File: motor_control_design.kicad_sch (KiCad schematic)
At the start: 90 parts, among them J1 TYPE-C-31-M-12, J10 5V, J2 SWD, J3 VBAT, J4 GND, J5 FC_M/P, J6 Conn_01x06, J7 Conn_01x04_Pin, J8 Conn_01x06, J9 GND, Q1 RF1S9540SM, Q10 2N7002, Q11 2N7002, Q12 2N7002, Q13 2N7002, Q14 RF1S9540SM, Q15 IRLZ44NS, Q16 2N7002, Q2 RF1S9540SM, Q3 IRLZ44NS, Q4 2N7002, Q5 2N7002, Q6 RF1S9540SM, Q7 IRLZ44NS, Q8 2N7002, Q9 IRLZ44NS, U1 STM32F401CCU6, U2 LT1962-3.3, U4 TPS563200, Y1 16MHz

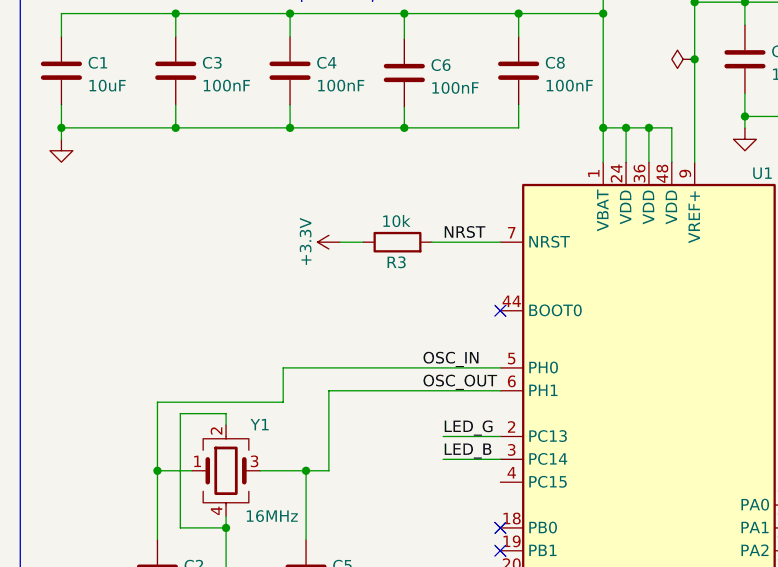
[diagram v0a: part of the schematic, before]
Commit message: cleaned up NRST BOOT0 schematic
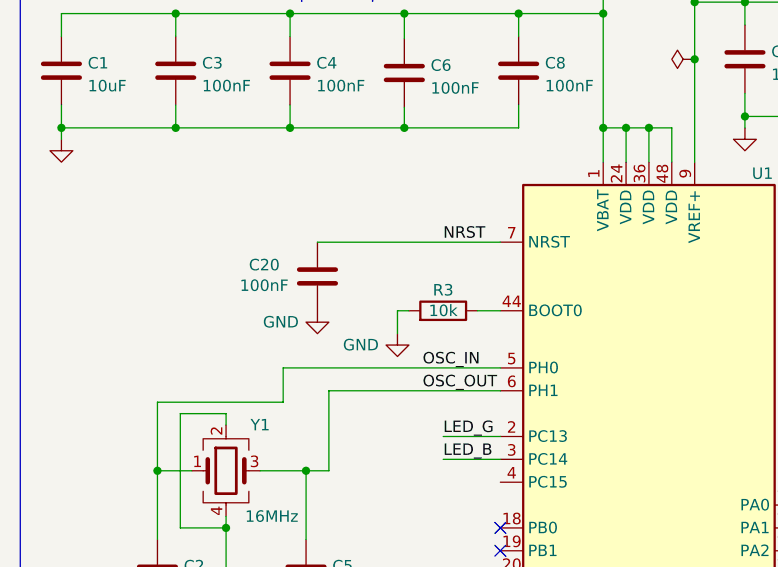
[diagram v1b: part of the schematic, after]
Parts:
- added C20: 100nF, symbol Device:C
- R3: LCSC Part C176114 -> C174364
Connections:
- net +3.3V: no longer R3.1
- net GND: now also R3.2, C20.2
- net NRST: now also C20.1; no longer R3.2
- net at U1.44 (BOOT0): now also R3.1
- no-connect marks 14 -> 13

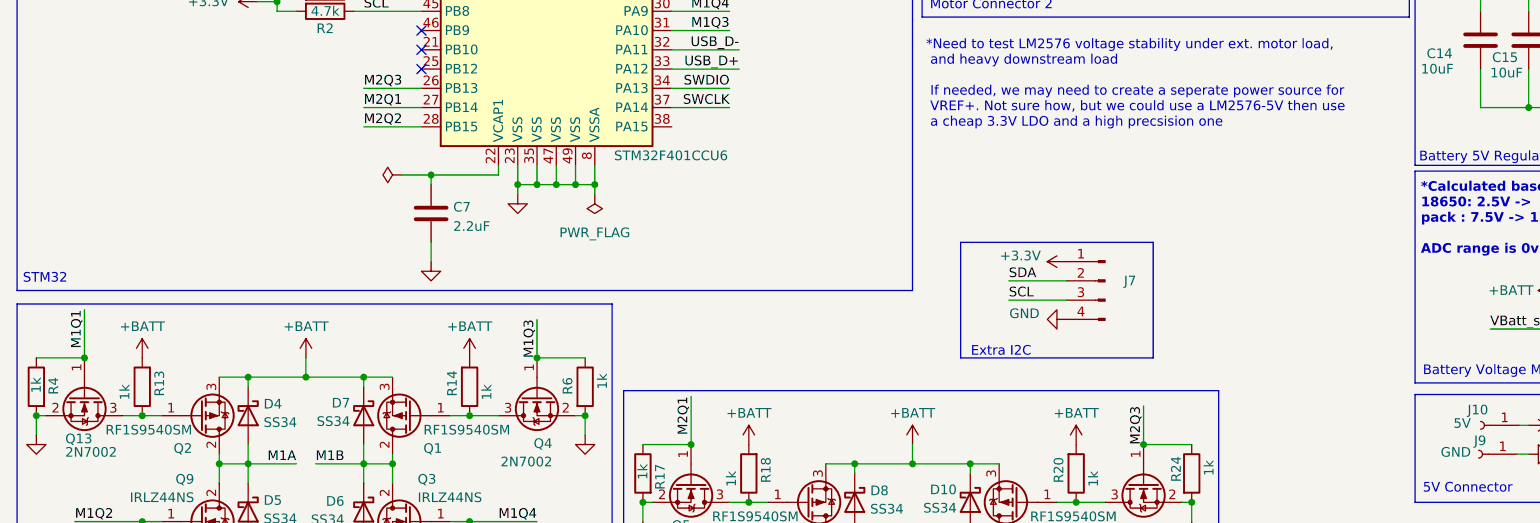
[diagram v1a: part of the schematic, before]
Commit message: Added LTC4365
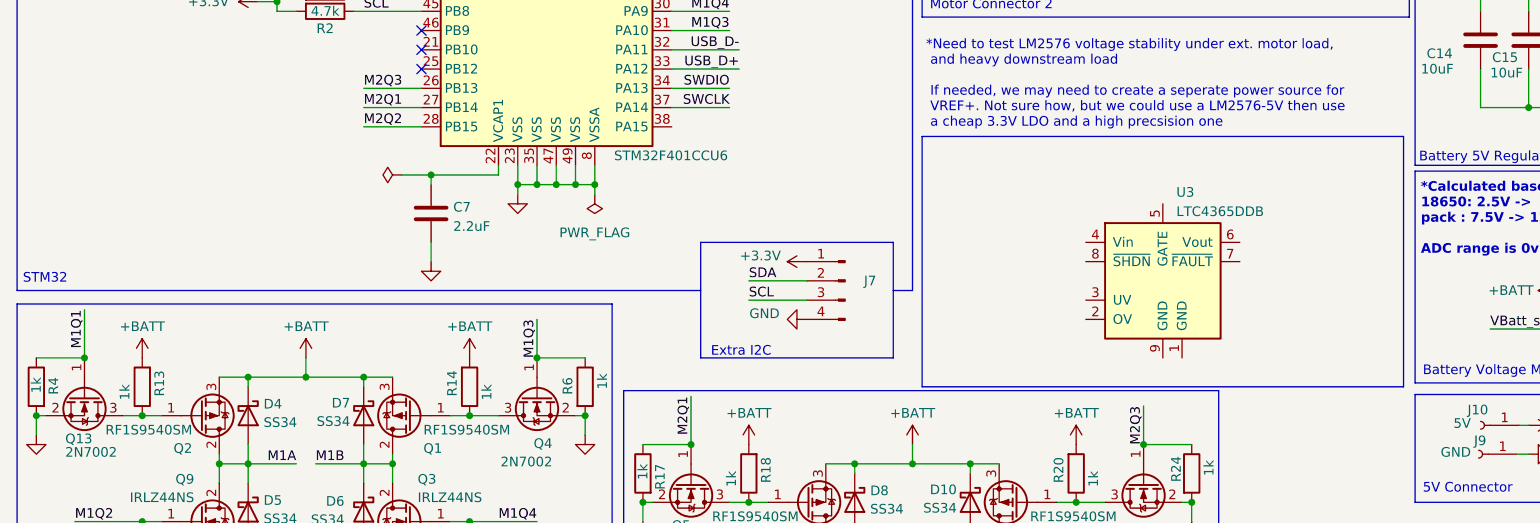
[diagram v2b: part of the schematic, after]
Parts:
- added U3: LTC4365DDB, Package_DFN_QFN:DFN-8-1EP_2x3mm_P0.5mm_EP0.61x2.2mm, symbol Power_Management:LTC4365DDB
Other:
- moved on the sheet: J7
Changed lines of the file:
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@@
 	)
 	(rectangle
+		(start 133.35 116.84)
+		(end 196.85 149.86)
+		(stroke
+			(width 0)
+			(type default)
+		)
+		(fill
+			(type none)
+		)
+	)
+	(rectangle
 		(start 133.35 68.58)
 		(end 197.612 101.092)
@@
 		)
 	)
-	(rectangle
-		(start 13.97 13.97)
-		(end 132.08 137.16)
-		(stroke
-			(width 0)
-			(type default)
-		)
-		(fill
-			(type none)
-		)
-	)
 	(text "Battery 5V Regulator"
 		(exclude_from_sim no)
@@
 	(text "Extra I2C\n"
 		(exclude_from_sim no)
-		(at 143.764 145.288 0)
+		(at 109.474 145.288 0)
 		(effects
 			(font
@@
 		)
 	)
+	(polyline
+		(pts
+			(xy 13.97 13.97) (xy 132.08 13.97)
+		)
+		(stroke
+			(width 0)
+			(type default)
+		)
+	)
 	(wire
 		(pts
@@
 	(wire
 		(pts
-			(xy 144.78 138.43) (xy 152.4 138.43)
+			(xy 110.49 138.43) (xy 118.11 138.43)
 		)
 		(stroke
@@
 	(polyline
 		(pts
-			(xy 138.43 146.05) (xy 163.83 146.05)
+			(xy 104.14 146.05) (xy 129.54 146.05)
 		)
 		(stroke
@@
 	(polyline
 		(pts
-			(xy 138.43 130.81) (xy 163.83 130.81)
+			(xy 104.14 130.81) (xy 129.54 130.81)
 		)
 		(stroke
@@
 		)
 	)
+	(polyline
+		(pts
+			(xy 13.97 137.16) (xy 104.14 137.16)
+		)
+		(stroke
+			(width 0)
+			(type default)
+		)
+	)
 	(wire
 		(pts
@@
 		)
 	)
+	(polyline
+		(pts
+			(xy 129.54 137.16) (xy 132.08 137.16)
+		)
+		(stroke
+			(width 0)
+			(type default)
+		)
+	)
 	(wire
 		(pts
@@
 	(wire
 		(pts
-			(xy 144.78 135.89) (xy 152.4 135.89)
+			(xy 110.49 135.89) (xy 118.11 135.89)
 		)
 		(stroke
@@
 		)
 	)
+	(polyline
+		(pts
+			(xy 13.97 137.16) (xy 13.97 13.97)
+		)
+		(stroke
+			(width 0)
+			(type default)
+		)
+	)
 	(wire
 		(pts
@@
 		)
 	)
+	(polyline
+		(pts
+			(xy 132.08 13.97) (xy 132.08 137.16)
+		)
+		(stroke
+			(width 0)
+			(type default)
+		)
+	)
 	(wire
 		(pts
@@
 	(polyline
 		(pts
-			(xy 138.43 130.81) (xy 138.43 146.05)
+			(xy 104.14 130.81) (xy 104.14 146.05)
 		)
 		(stroke
@@
 	(polyline
 		(pts
-			(xy 163.83 146.05) (xy 163.83 130.81)
+			(xy 129.54 146.05) (xy 129.54 130.81)
 		)
 		(stroke
@@
 	)
 	(label "SCL"
-		(at 144.78 138.43 0)
+		(at 110.49 138.43 0)
 		(effects
 			(font
@@
 	)
 	(label "SDA"
-		(at 144.78 135.89 0)
+		(at 110.49 135.89 0)
 		(effects
 			(font
@@
 	)
 	(symbol
+		(lib_id "Power_Management:LTC4365DDB")
+		(at 165.1 135.89 0)
+		(unit 1)
+		(exclude_from_sim no)
+		(in_bom yes)
+		(on_board yes)
+		(dnp no)
+		(property "Reference" "U3"
+			(at 166.878 124.206 0)
+			(effects
+				(font
+					(size 1.27 1.27)
+				)
+				(justify left)
+			)
+		)
+		(property "Value" "LTC4365DDB"
+			(at 166.878 126.746 0)
+			(effects
+				(font
+					(size 1.27 1.27)
+				)
+				(justify left)
+			)
+		)
+		(property "Footprint" "Package_DFN_QFN:DFN-8-1EP_2x3mm_P0.5mm_EP0.61x2.2mm"
+			(at 165.1 148.59 0)
+			(effects
+				(font
+					(size 1.27 1.27)
+				)
+				(hide yes)
+			)
+		)
+		(property "Datasheet" "https://www.analog.com/media/en/technical-documentation/data-sheets/4365fa.pdf"
+			(at 165.1 133.35 0)
+			(effects
+				(font
+					(size 1.27 1.27)
+				)
+				(hide yes)
+			)
+		)
+		(property "Description" "UV, OV and Reverse Supply Protection Controller, 50/60Hz noise rejection, DFN-8"
+			(at 165.1 135.89 0)
+			(effects
+				(font
+					(size 1.27 1.27)
+				)
+				(hide yes)
+			)
+		)
+		(pin "4"
+		)
+		(pin "3"
+		)
+		(pin "8"
+		)
+		(pin "6"
+		)
+		(pin "9"
+		)
+		(pin "7"
+		)
+		(pin "1"
+		)
+		(pin "5"
+		)
+		(pin "2"
+		)
+		(instances
+			(project ""
+				(path "/e96577c4-ec21-4b26-996c-9ebc38d9c737"
+					(reference "U3")
+					(unit 1)
+				)
+			)
+		)
+	)
+	(symbol
 		(lib_id "power:GND")
 		(at 144.78 91.44 90)
@@
 	(symbol
 		(lib_id "Connector:Conn_01x04_Pin")
-		(at 157.48 135.89 0)
+		(at 123.19 135.89 0)
 		(mirror y)
 		(unit 1)
@@
 		(dnp no)
 		(property "Reference" "J7"
-			(at 160.782 135.89 0)
+			(at 126.492 135.89 0)
 			(effects
 				(font
@@
 		)
 		(property "Value" "Conn_01x04_Pin"
-			(at 156.845 130.81 0)
+			(at 122.555 130.81 0)
 			(effects
 				(font
@@
 		)
 		(property "Footprint" "Connector_JST:JST_SH_BM04B-SRSS-TB_1x04-1MP_P1.00mm_Vertical"
-			(at 157.48 135.89 0)
+			(at 123.19 135.89 0)
 			(effects
 				(font
@@
 		)
 		(property "Datasheet" "~"
-			(at 157.48 135.89 0)
+			(at 123.19 135.89 0)
 			(effects
 				(font
@@
 		)
 		(property "Description" "Generic connector, single row, 01x04, script generated"
-			(at 157.48 135.89 0)
+			(at 123.19 135.89 0)
 			(effects
 				(font
@@
 		)
 		(property "LCSC Part" "C160390"
-			(at 157.48 135.89 0)
+			(at 123.19 135.89 0)
 			(effects
 				(font
@@
 	(symbol
 		(lib_id "power:+3.3V")
-		(at 152.4 133.35 90)
+		(at 118.11 133.35 90)
 		(mirror x)
 		(unit 1)
@@
 		(dnp no)
 		(property "Reference" "#PWR031"
-			(at 156.21 133.35 0)
+			(at 121.92 133.35 0)
 			(effects
 				(font
@@
 		)
 		(property "Value" "+3.3V"
-			(at 146.304 132.588 90)
+			(at 112.014 132.588 90)
 			(effects
 				(font
@@
 		)
 		(property "Footprint" ""
-			(at 152.4 133.35 0)
+			(at 118.11 133.35 0)
 			(effects
 				(font
@@
 		)
 		(property "Datasheet" ""
-			(at 152.4 133.35 0)
+			(at 118.11 133.35 0)
 			(effects
 				(font
@@
 		)
 		(property "Description" ""
-			(at 152.4 133.35 0)
+			(at 118.11 133.35 0)
 			(effects
 				(font
@@
 		(lib_name "GND_6")
 		(lib_id "power:GND")
-		(at 152.4 140.97 270)
+		(at 118.11 140.97 270)
 		(unit 1)
 		(exclude_from_sim no)
@@
 		(dnp no)
 		(property "Reference" "#PWR032"
-			(at 146.05 140.97 0)
+			(at 111.76 140.97 0)
 			(effects
 				(font
@@
 		)
 		(property "Value" "GND"
-			(at 148.844 140.208 90)
+			(at 114.554 140.208 90)
 			(effects
 				(font
@@
 		)
 		(property "Footprint" ""
-			(at 152.4 140.97 0)
+			(at 118.11 140.97 0)
 			(effects
 				(font
@@
 		)
 		(property "Datasheet" ""
-			(at 152.4 140.97 0)
+			(at 118.11 140.97 0)
 			(effects
 				(font
@@
 		)
 		(property "Description" "Power symbol creates a global label with name \"GND\" , ground"
-			(at 152.4 140.97 0)
+			(at 118.11 140.97 0)
 			(effects
 				(font

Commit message: Overvoltage system schematic drafted
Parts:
- added R29, R30: R, symbol Device:R
- added U5: SSM6N7002KFU_LF, SOT-363 US6_TOS, symbol Custom:SSM6N7002KFU_LF
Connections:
- net +BATT: now also U3.3 (UV), U3.4 (Vin), R29.1, U5.3 (DRAIN2); no longer D4.1 (K), D7.1 (K), Q1.3 (S), Q2.3 (S), R18.2
- net GND: now also U3.1 (GND), U3.9 (GND), R30.2
- net at U3.2 (OV): now also R29.2, R30.1
- net at U3.5 (GATE): now also U5.2 (GATE1), U5.5 (GATE2)
- net at U3.6 (Vout): now also U5.6 (DRAIN1)
- new net: D4.1 (K), D7.1 (K), Q1.3 (S), Q2.3 (S)
- new net: U5.1 (SOURCE1), U5.4 (SOURCE2)
- no-connect marks 13 -> 14
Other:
- note removed: "*Need to test LM2576 voltage stability under ext. motor load, and heavy downstream load If needed, we may need to create a seperate power source for VREF+. Not sure how, but we could use a LM2576-5V then use a cheap 3.3V LDO and a high precsision one"
- moved on the sheet: U3

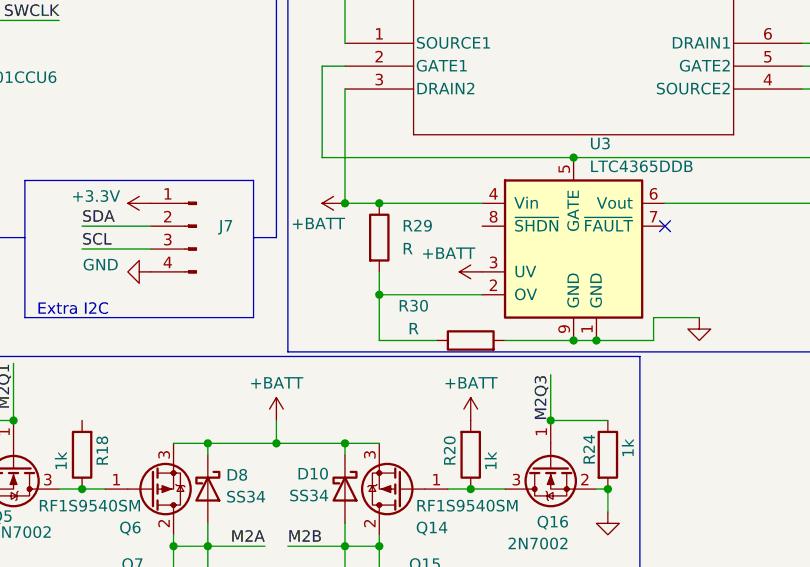
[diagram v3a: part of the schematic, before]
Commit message: updated overvoltage resistor values
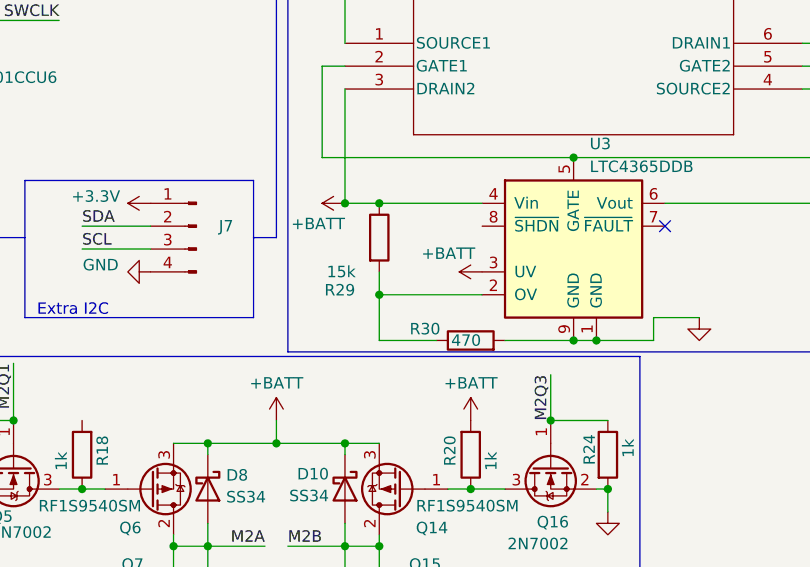
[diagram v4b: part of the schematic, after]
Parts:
- R29: value R -> 15k
- R30: value R -> 470
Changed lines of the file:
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@@
 		(on_board yes)
 		(dnp no)
-		(fields_autoplaced yes)
 		(property "Reference" "R29"
-			(at 146.05 135.8899 0)
-			(effects
-				(font
-					(size 1.27 1.27)
-				)
-				(justify left)
-			)
-		)
-		(property "Value" "R"
-			(at 146.05 138.4299 0)
+			(at 137.414 143.002 0)
+			(effects
+				(font
+					(size 1.27 1.27)
+				)
+				(justify left)
+			)
+		)
+		(property "Value" "15k"
+			(at 137.668 140.97 0)
 			(effects
 				(font
@@
 		(dnp no)
 		(property "Reference" "R30"
-			(at 147.32 144.78 90)
-			(effects
-				(font
-					(size 1.27 1.27)
-				)
-			)
-		)
-		(property "Value" "R"
-			(at 147.32 147.32 90)
-			(effects
-				(font
+			(at 148.59 147.32 90)
+			(effects
+				(font
+					(size 1.27 1.27)
+				)
+			)
+		)
+		(property "Value" "470"
+			(at 153.162 148.59 90)
+			(effects
+				(font

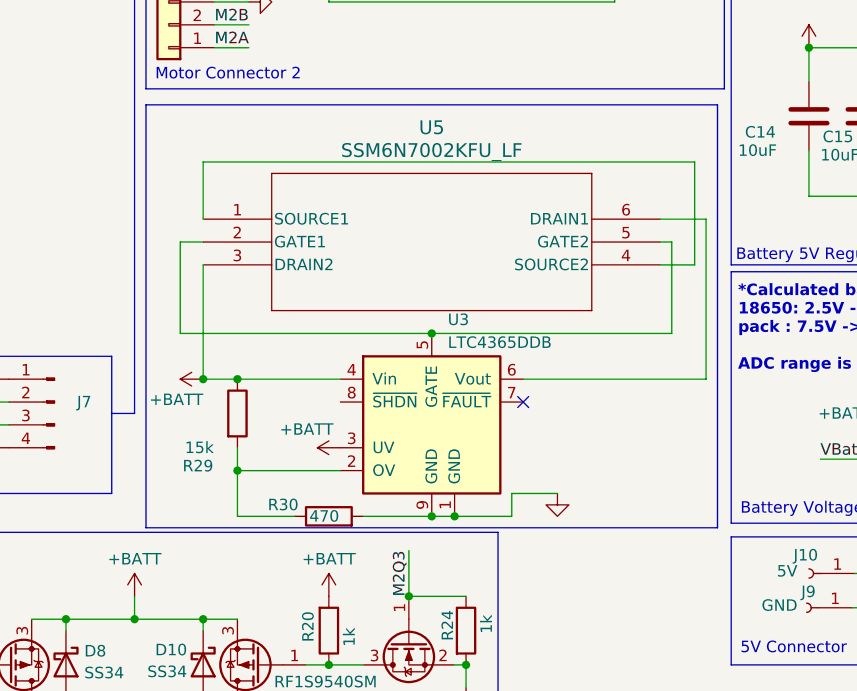
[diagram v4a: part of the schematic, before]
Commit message: connected shdn
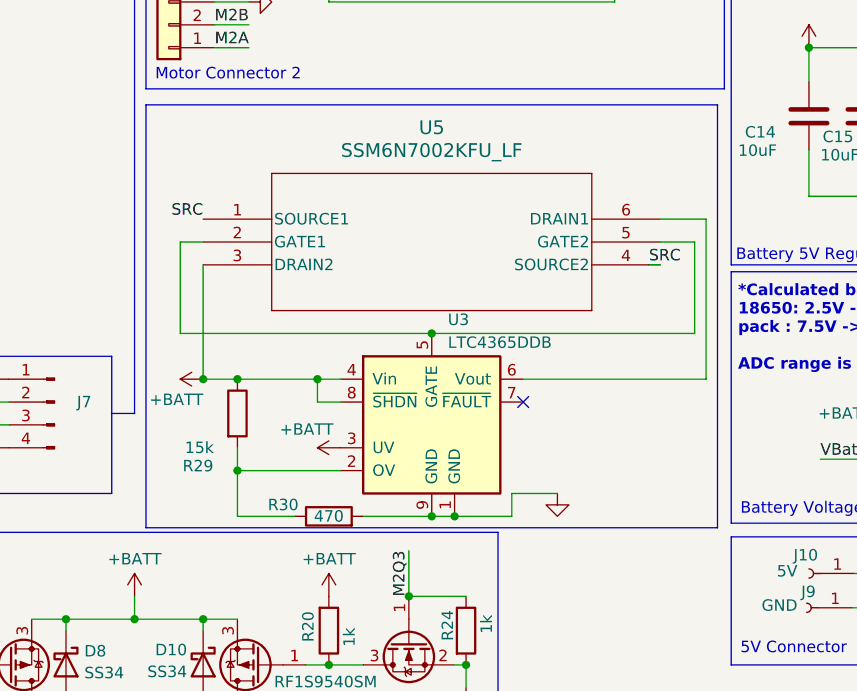
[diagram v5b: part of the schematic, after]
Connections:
- net +BATT: now also U3.8 (~{SHDN})
- net SRC: now reaches U5.1 (SOURCE1), U5.4 (SOURCE2)
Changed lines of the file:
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@@
 	)
 	(junction
+		(at 152.4 133.35)
+		(diameter 0)
+		(color 0 0 0 0)
+	)
+	(junction
 		(at 260.35 105.41)
 		(diameter 0)
@@
 	(wire
 		(pts
-			(xy 190.5 118.11) (xy 191.77 118.11)
+			(xy 190.5 118.11) (xy 194.31 118.11)
 		)
 		(stroke
@@
 	(wire
 		(pts
-			(xy 191.77 128.27) (xy 165.1 128.27)
+			(xy 194.31 128.27) (xy 165.1 128.27)
 		)
 		(stroke
@@
 	(wire
 		(pts
-			(xy 139.7 109.22) (xy 139.7 115.57)
-		)
-		(stroke
-			(width 0)
-			(type default)
-		)
-	)
-	(wire
-		(pts
 			(xy 143.51 143.51) (xy 154.94 143.51)
 		)
@@
 	(wire
 		(pts
-			(xy 191.77 118.11) (xy 191.77 128.27)
+			(xy 194.31 118.11) (xy 194.31 128.27)
 		)
 		(stroke
@@
 	(wire
 		(pts
-			(xy 194.31 109.22) (xy 139.7 109.22)
-		)
-		(stroke
-			(width 0)
-			(type default)
-		)
-	)
-	(wire
-		(pts
 			(xy 48.26 97.79) (xy 50.8 97.79)
 		)
@@
 		)
 	)
+	(wire
+		(pts
+			(xy 152.4 133.35) (xy 154.94 133.35)
+		)
+		(stroke
+			(width 0)
+			(type default)
+		)
+	)
 	(polyline
 		(pts
@@
 	(wire
 		(pts
-			(xy 190.5 120.65) (xy 194.31 120.65)
-		)
-		(stroke
-			(width 0)
-			(type default)
-		)
-	)
-	(wire
-		(pts
 			(xy 96.52 167.64) (xy 96.52 165.1)
 		)
@@
 	(wire
 		(pts
+			(xy 189.23 120.65) (xy 190.5 120.65)
+		)
+		(stroke
+			(width 0)
+			(type default)
+		)
+	)
+	(wire
+		(pts
 			(xy 139.7 181.61) (xy 139.7 184.15)
 		)
@@
 	(wire
 		(pts
+			(xy 154.94 135.89) (xy 152.4 135.89)
+		)
+		(stroke
+			(width 0)
+			(type default)
+		)
+	)
+	(wire
+		(pts
 			(xy 58.42 100.33) (xy 67.31 100.33)
 		)
@@
 	(wire
 		(pts
+			(xy 152.4 133.35) (xy 152.4 135.89)
+		)
+		(stroke
+			(width 0)
+			(type default)
+		)
+	)
+	(wire
+		(pts
 			(xy 59.69 160.02) (xy 53.34 160.02)
 		)
@@
 	(wire
 		(pts
-			(xy 143.51 133.35) (xy 154.94 133.35)
+			(xy 143.51 133.35) (xy 152.4 133.35)
 		)
 		(stroke
@@
 	(wire
 		(pts
-			(xy 194.31 120.65) (xy 194.31 109.22)
-		)
-		(stroke
-			(width 0)
-			(type default)
-		)
-	)
-	(wire
-		(pts
 			(xy 227.33 106.68) (xy 227.33 113.03)
 		)
@@
 		)
 	)
+	(label "SRC"
+		(at 189.23 120.65 0)
+		(effects
+			(font
+				(size 1.27 1.27)
+			)
+			(justify left bottom)
+		)
+	)
 	(label "OSC_OUT"
 		(at 58.674 64.77 0)
@@
 		)
 	)
+	(label "SRC"
+		(at 139.7 115.57 180)
+		(effects
+			(font
+				(size 1.27 1.27)
+			)
+			(justify right bottom)
+		)
+	)
 	(label "E1A"
 		(at 60.96 87.63 0)
@@
 		)
 		(property "Value" "470"
-			(at 153.162 148.59 90)
+			(at 153.67 148.59 90)
 			(effects
 				(font
